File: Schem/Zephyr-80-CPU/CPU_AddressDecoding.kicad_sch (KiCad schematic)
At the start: 16 parts, among them U1 AS7C4096A-12TCN, U2 ATF22V10C-10PU, U3 Z084000xP, U4 SST39SF040-70-4C-PHE, U5 ATF22V10C-10PU, U6 SN74HC273DWR, U7 SN74HC244DWR, Y1 ECS-2100AX-100

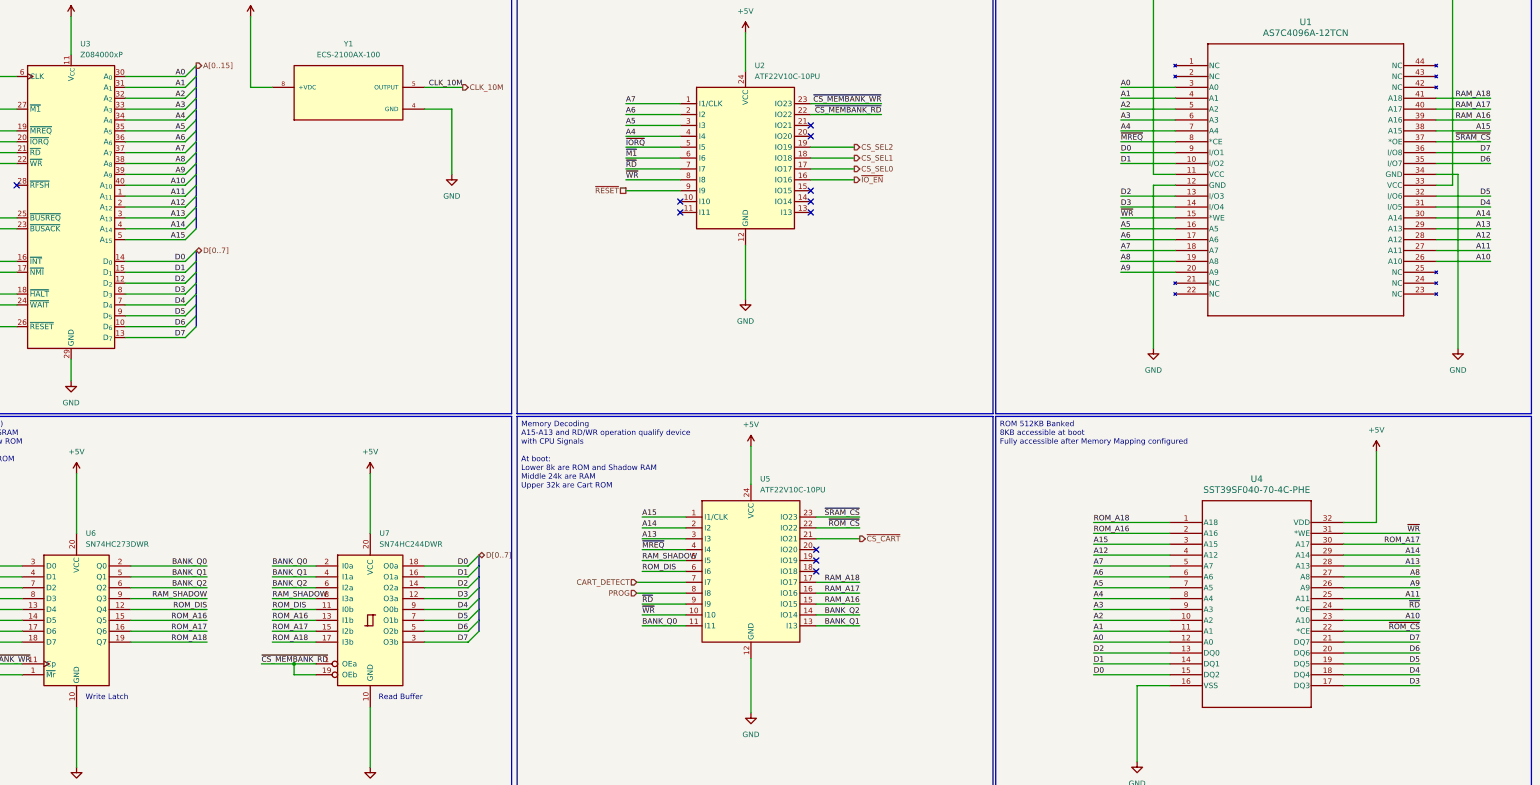
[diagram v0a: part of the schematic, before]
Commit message: Routed the CPU board. Removed the rotary switches decoder
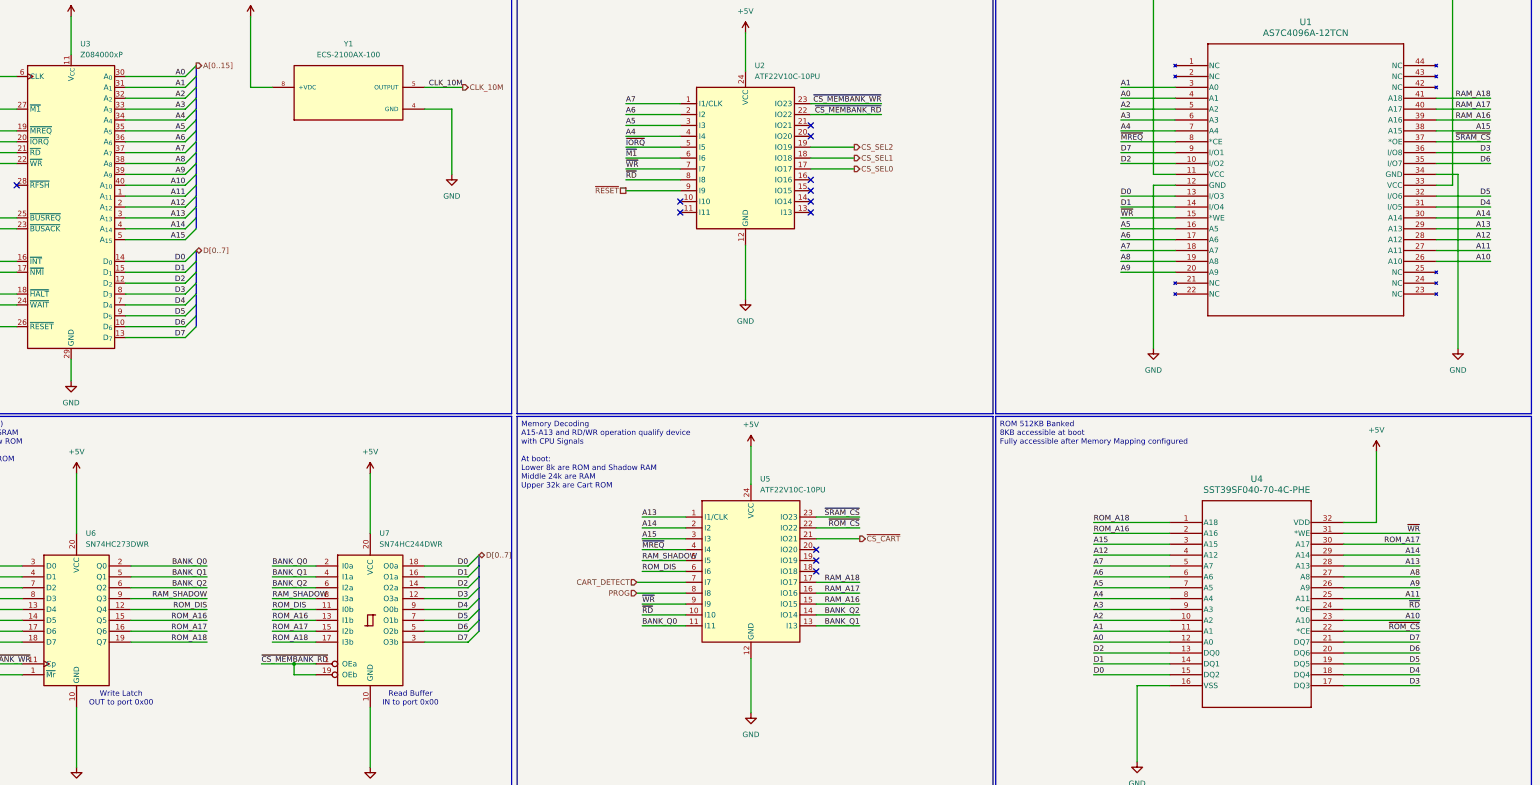
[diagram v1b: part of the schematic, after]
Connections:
- net A0: now also U1.4 (A1); no longer U1.3 (A0)
- net A1: now also U1.3 (A0); no longer U1.4 (A1)
- net A13: now also U5.1 (I1/CLK); no longer U5.3 (I3)
- net A15: now also U5.3 (I3); no longer U5.1 (I1/CLK)
- net D0: now also U1.13 (I/O3); no longer U1.9 (I/O1)
- net D1: now also U1.14 (I/O4); no longer U1.10 (I/O2)
- net D2: now also U1.10 (I/O2); no longer U1.13 (I/O3)
- net D3: now also U1.36 (I/O8); no longer U1.14 (I/O4)
- net D7: now also U1.9 (I/O1); no longer U1.36 (I/O8)
- net ~{RD}: now also U2.8 (I8), U5.10 (I10); no longer U2.7 (I7), U5.9 (I9)
- net ~{WR}: now also U2.7 (I7), U5.9 (I9); no longer U2.8 (I8), U5.10 (I10)
- net ~{IO_EN}: no longer names the net of U2.16 (IO16)
- no-connect marks 11 -> 12
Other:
- note added: "Read Buffer IN to port 0x00"
- note added: "Write Latch OUT to port 0x00"
- note removed: "Read Buffer"
- note removed: "Write Latch"
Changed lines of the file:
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@@
 	(generator_version "9.0")
 	(paper "USLedger")
-	(text "Write Latch"
+	(text "Write Latch\nOUT to port 0x00"
 		(exclude_from_sim no)
-		(at 65.532 194.564 0)
+		(at 68.834 194.818 0)
 		(effects
 			(font
@@
 		)
 	)
-	(text "Read Buffer"
+	(text "Read Buffer\nIN to port 0x00"
 		(exclude_from_sim no)
-		(at 134.112 194.564 0)
+		(at 136.398 194.818 0)
 		(effects
 			(font
@@
 	)
 	(no_connect
+		(at 229.87 73.66)
+	)
+	(no_connect
 		(at 229.87 60.96)
 	)
@@
 	(wire
 		(pts
-			(xy 229.87 73.66) (xy 240.03 73.66)
-		)
-		(stroke
-			(width 0)
-			(type default)
-		)
-	)
-	(wire
-		(pts
 			(xy 149.86 179.07) (xy 139.7 179.07)
 		)
@@
 	)
 	(label "~{WR}"
-		(at 186.69 73.66 0)
+		(at 186.69 71.12 0)
 		(effects
 			(font
@@
 	)
 	(label "A0"
-		(at 302.26 52.07 0)
+		(at 302.26 54.61 0)
 		(effects
 			(font
@@
 	)
 	(label "~{RD}"
-		(at 186.69 71.12 0)
+		(at 186.69 73.66 0)
 		(effects
 			(font
@@
 	)
 	(label "A1"
-		(at 302.26 54.61 0)
+		(at 302.26 52.07 0)
 		(effects
 			(font
@@
 	)
 	(label "D0"
-		(at 302.26 67.31 0)
+		(at 302.26 77.47 0)
 		(effects
 			(font
@@
 	)
 	(label "D1"
-		(at 302.26 69.85 0)
+		(at 302.26 80.01 0)
 		(effects
 			(font
@@
 	)
 	(label "D3"
-		(at 302.26 80.01 0)
+		(at 388.62 67.31 180)
 		(effects
 			(font
 				(size 1.27 1.27)
 			)
-			(justify left bottom)
+			(justify right bottom)
 		)
 	)
@@
 	)
 	(label "A15"
-		(at 190.5 152.4 0)
+		(at 190.5 157.48 0)
 		(effects
 			(font
@@
 	)
 	(label "D2"
-		(at 302.26 77.47 0)
+		(at 302.26 69.85 0)
 		(effects
 			(font
@@
 	)
 	(label "~{RD}"
-		(at 190.5 172.72 0)
+		(at 190.5 175.26 0)
 		(effects
 			(font
@@
 	)
 	(label "~{WR}"
-		(at 190.5 175.26 0)
+		(at 190.5 172.72 0)
 		(effects
 			(font
@@
 	)
 	(label "D7"
-		(at 388.62 67.31 180)
+		(at 302.26 67.31 0)
 		(effects
 			(font
 				(size 1.27 1.27)
 			)
-			(justify right bottom)
+			(justify left bottom)
 		)
 	)
@@
 	)
 	(label "A13"
-		(at 190.5 157.48 0)
+		(at 190.5 152.4 0)
 		(effects
 			(font
@@
 		(effects
 			(font
-				(size 1.27 1.27)
-			)
-			(justify left)
-		)
-	)
-	(hierarchical_label "~{IO_EN}"
-		(shape output)
-		(at 240.03 73.66 0)
-		(effects
-			(font

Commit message: Added all the manufacturer part numbers to the KiCad schematics and PCB files. This will make it easier to order the parts for the project and ensure that the correct components are used. I also removed some of the old schematics that were no longer needed, such as the BaudClock, ConsolePort, DeviceSelectDecode, GPIOUserSerial, IO Controller, UserPorts, Video, and Z80HomeBrew schematics. These changes will help to streamline the design and make it easier to understand.
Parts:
- C1, C2, C3, C4, C5, C6, C7, C8: footprint Capacitor_SMD:C_0805_2012Metric -> Capacitor_SMD:C_0603_1608Metric; MANUFACTURER_PART_NUMBER 0402B104K160CT -> 0603B104K160CT
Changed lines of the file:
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@@
 			)
 		)
-		(property "Footprint" "Capacitor_SMD:C_0805_2012Metric"
+		(property "Footprint" "Capacitor_SMD:C_0603_1608Metric"
 			(at 68.2752 243.84 0)
 			(effects
@@
 			)
 		)
-		(property "MANUFACTURER_PART_NUMBER" "0402B104K160CT"
+		(property "MANUFACTURER_PART_NUMBER" "0603B104K160CT"
 			(at 67.31 240.03 0)
 			(effects
@@
 			)
 		)
-		(property "Footprint" "Capacitor_SMD:C_0805_2012Metric"
+		(property "Footprint" "Capacitor_SMD:C_0603_1608Metric"
 			(at 44.1452 243.84 0)
 			(effects
@@
 			)
 		)
-		(property "MANUFACTURER_PART_NUMBER" "0402B104K160CT"
+		(property "MANUFACTURER_PART_NUMBER" "0603B104K160CT"
 			(at 43.18 240.03 0)
 			(effects
@@
 			)
 		)
-		(property "Footprint" "Capacitor_SMD:C_0805_2012Metric"
+		(property "Footprint" "Capacitor_SMD:C_0603_1608Metric"
 			(at 78.4352 243.84 0)
 			(effects
@@
 			)
 		)
-		(property "MANUFACTURER_PART_NUMBER" "0402B104K160CT"
+		(property "MANUFACTURER_PART_NUMBER" "0603B104K160CT"
 			(at 77.47 240.03 0)
 			(effects
@@
 			)
 		)
-		(property "Footprint" "Capacitor_SMD:C_0805_2012Metric"
+		(property "Footprint" "Capacitor_SMD:C_0603_1608Metric"
 			(at 102.5652 243.84 0)
 			(effects
@@
 			)
 		)
-		(property "MANUFACTURER_PART_NUMBER" "0402B104K160CT"
+		(property "MANUFACTURER_PART_NUMBER" "0603B104K160CT"
 			(at 101.6 240.03 0)
 			(effects
@@
 			)
 		)
-		(property "Footprint" "Capacitor_SMD:C_0805_2012Metric"
+		(property "Footprint" "Capacitor_SMD:C_0603_1608Metric"
 			(at 113.9952 243.84 0)
 			(effects
@@
 			)
 		)
-		(property "MANUFACTURER_PART_NUMBER" "0402B104K160CT"
+		(property "MANUFACTURER_PART_NUMBER" "0603B104K160CT"
 			(at 113.03 240.03 0)
 			(effects
@@
 			)
 		)
-		(property "Footprint" "Capacitor_SMD:C_0805_2012Metric"
+		(property "Footprint" "Capacitor_SMD:C_0603_1608Metric"
 			(at 125.4252 243.84 0)
 			(effects
@@
 			)
 		)
-		(property "MANUFACTURER_PART_NUMBER" "0402B104K160CT"
+		(property "MANUFACTURER_PART_NUMBER" "0603B104K160CT"
 			(at 124.46 240.03 0)
 			(effects
@@
 			)
 		)
-		(property "Footprint" "Capacitor_SMD:C_0805_2012Metric"
+		(property "Footprint" "Capacitor_SMD:C_0603_1608Metric"
 			(at 91.1352 243.84 0)
 			(effects
@@
 			)
 		)
-		(property "MANUFACTURER_PART_NUMBER" "0402B104K160CT"
+		(property "MANUFACTURER_PART_NUMBER" "0603B104K160CT"
 			(at 90.17 240.03 0)
 			(effects
@@
 			)
 		)
-		(property "Footprint" "Capacitor_SMD:C_0805_2012Metric"
+		(property "Footprint" "Capacitor_SMD:C_0603_1608Metric"
 			(at 56.8452 243.84 0)
 			(effects
@@
 			)
 		)
-		(property "MANUFACTURER_PART_NUMBER" "0402B104K160CT"
+		(property "MANUFACTURER_PART_NUMBER" "0603B104K160CT"
 			(at 55.88 240.03 0)
 			(effects
